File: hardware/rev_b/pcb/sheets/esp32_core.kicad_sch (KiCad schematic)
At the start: 33 parts, among them J4 TC2030 recovery pads, SW1 SKRABCE010, SW2 SKRABCE010, U1 ESP32-S3-WROOM-1-N16

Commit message: feat(hw): simplify Rev B controls with purchased Omron caps
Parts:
- SW1, SW2: value SKRABCE010 -> B3F-4050; footprint cicala:SW_Alps_SKRABCE010 -> cicala:SW_Omron_B3F-4050; MPN SKRABCE010 -> B3F-4050; Manufacturer Alps Alpine -> Omron
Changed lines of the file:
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@@
 			)
 		)
-		(property "Value" "SKRABCE010"
+		(property "Value" "B3F-4050"
 			(at 168.91 46.482 0)
 			(show_name no)
@@
 			)
 		)
-		(property "Footprint" "cicala:SW_Alps_SKRABCE010"
+		(property "Footprint" "cicala:SW_Omron_B3F-4050"
 			(at 168.91 52.07 0)
 			(hide yes)
@@
 			)
 		)
-		(property "Datasheet" "https://tech.alpsalpine.com/e/products/detail/SKRABCE010/"
+		(property "Datasheet" "https://omronfs.omron.com/en_US/ecb/products/pdf/en-b3f.pdf"
 			(at 168.91 52.07 0)
 			(hide yes)
@@
 			)
 		)
-		(property "MPN" "SKRABCE010"
+		(property "MPN" "B3F-4050"
 			(at 168.91 52.07 0)
 			(hide yes)
@@
 			)
 		)
-		(property "Manufacturer" "Alps Alpine"
+		(property "Manufacturer" "Omron"
 			(at 168.91 52.07 0)
 			(hide yes)
@@
 			)
 		)
-		(property "Value" "SKRABCE010"
+		(property "Value" "B3F-4050"
 			(at 27.94 55.88 0)
 			(show_name no)
@@
 			)
 		)
-		(property "Footprint" "cicala:SW_Alps_SKRABCE010"
+		(property "Footprint" "cicala:SW_Omron_B3F-4050"
 			(at 27.94 62.23 0)
 			(hide yes)
@@
 			)
 		)
-		(property "Datasheet" "https://tech.alpsalpine.com/e/products/detail/SKRABCE010/"
+		(property "Datasheet" "https://omronfs.omron.com/en_US/ecb/products/pdf/en-b3f.pdf"
 			(at 27.94 62.23 0)
 			(hide yes)
@@
 			)
 		)
-		(property "MPN" "SKRABCE010"
+		(property "MPN" "B3F-4050"
 			(at 27.94 62.23 0)
 			(hide yes)
@@
 			)
 		)
-		(property "Manufacturer" "Alps Alpine"
+		(property "Manufacturer" "Omron"
 			(at 27.94 62.23 0)
 			(hide yes)

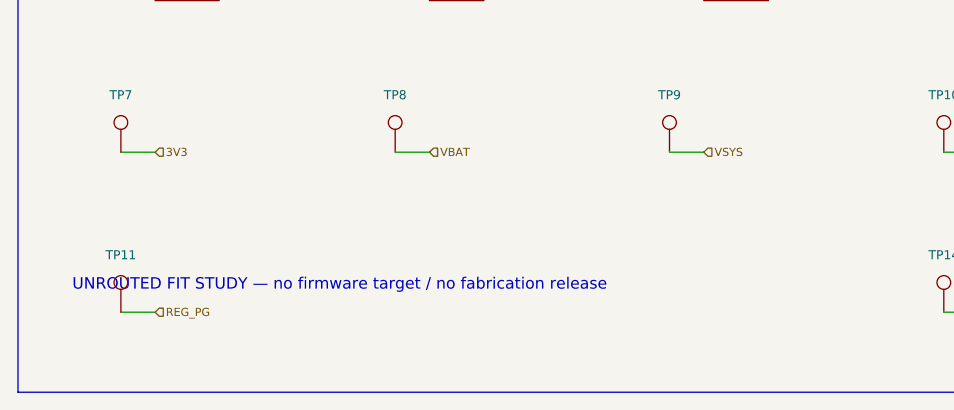
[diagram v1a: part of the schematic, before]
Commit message: fix(hw): recess Rev B controls and prepare first-article files
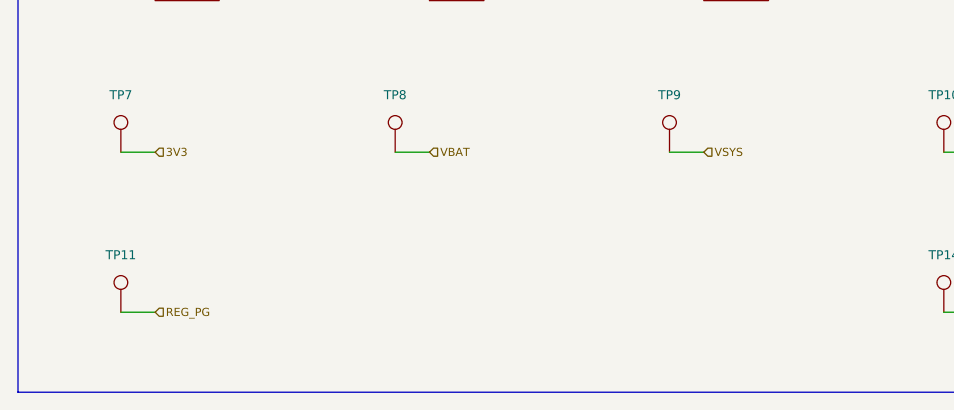
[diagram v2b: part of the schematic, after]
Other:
- note removed: "UNROUTED FIT STUDY — no firmware target / no fabrication release"
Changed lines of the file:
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@@
 	(title_block
 		(title "Controller, user I/O, and recovery")
-		(date "2026-09-07")
-		(rev "Rev B FIT - NOT FOR FABRICATION")
+		(date "2026-09-16")
+		(rev "B.05")
 		(company "Cicala")
+		(comment 1 "Engineering prototype; physical qualification pending")
 	)
 	(rectangle
@@
 		)
 	)
-	(text "UNROUTED FIT STUDY — no firmware target / no fabrication release"
-		(at 20 185 0)
-		(effects
-			(font
-				(size 1.27 1.27)
-			)
-			(justify left)
-		)
-	)
